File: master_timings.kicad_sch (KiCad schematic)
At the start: 9 parts, among them U1 74LS169BN, U11 TBP18s030, U12 74LS174N, U3 74F04, Y1 14 Mhz

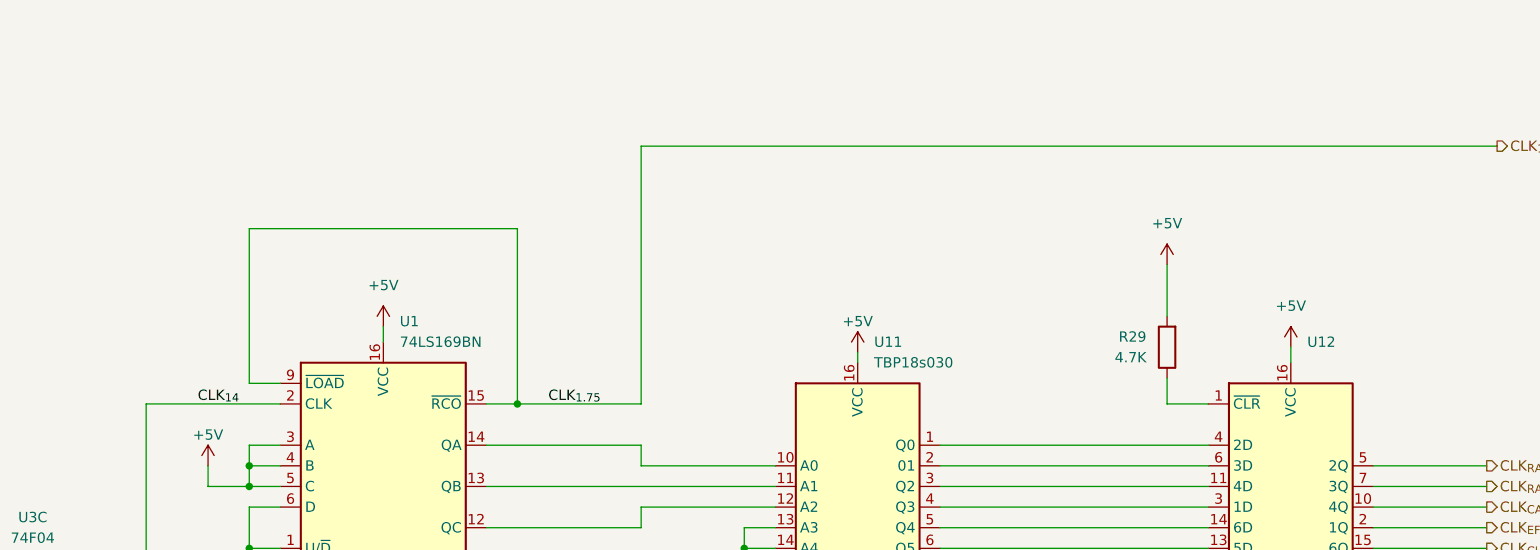
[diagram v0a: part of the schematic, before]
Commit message: Improved signal naming
clearer naming of some signals for better readability
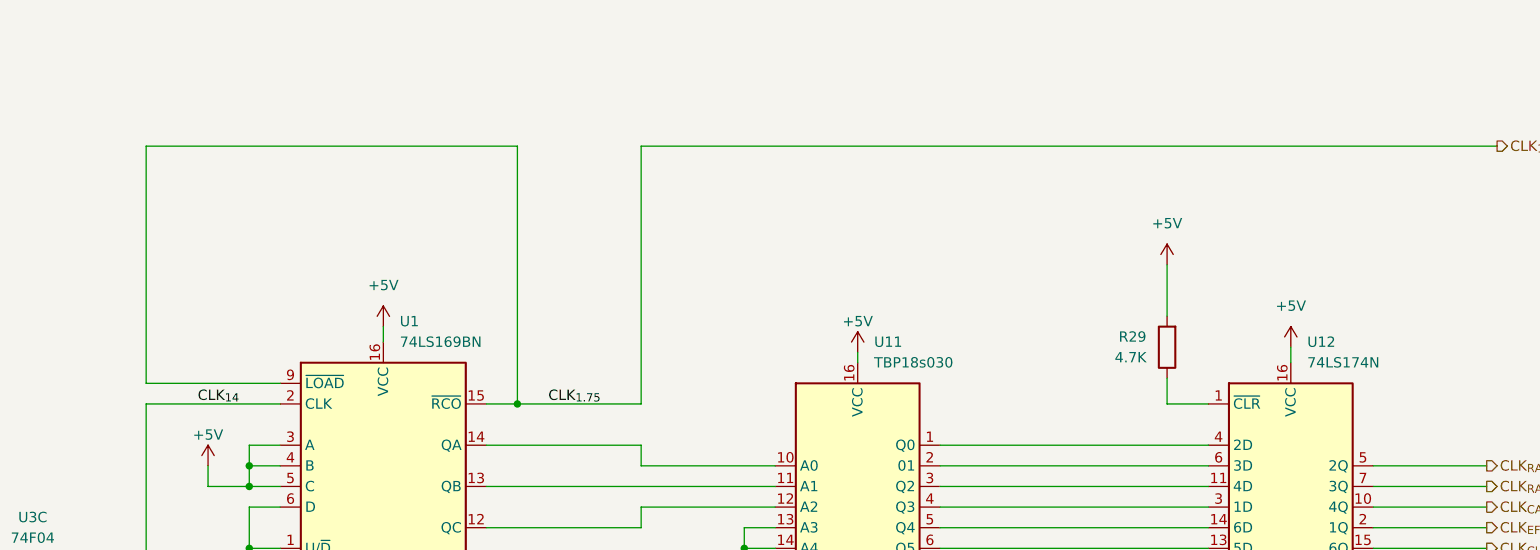
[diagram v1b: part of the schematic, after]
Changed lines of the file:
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@@
     (stroke (width 0) (type default))
   )
-  (wire (pts (xy 104.14 96.52) (xy 104.14 77.47))
+  (wire (pts (xy 91.44 96.52) (xy 91.44 67.31))
     (stroke (width 0) (type default))
   )
@@
     (stroke (width 0) (type default))
   )
-  (wire (pts (xy 104.14 96.52) (xy 107.95 96.52))
+  (wire (pts (xy 91.44 96.52) (xy 107.95 96.52))
     (stroke (width 0) (type default))
   )
@@
     (stroke (width 0) (type default))
   )
-  (wire (pts (xy 137.16 99.06) (xy 137.16 77.47))
+  (wire (pts (xy 137.16 99.06) (xy 137.16 67.31))
     (stroke (width 0) (type default))
   )
@@
     (stroke (width 0) (type default))
   )
-  (wire (pts (xy 104.14 77.47) (xy 137.16 77.47))
+  (wire (pts (xy 91.44 67.31) (xy 137.16 67.31))
     (stroke (width 0) (type default))
   )
@@
     )
     (property "Value" "74LS174N" (at 234.4294 93.98 0)
-      (effects (font (size 1.27 1.27)) (justify left) hide)
+      (effects (font (size 1.27 1.27)) (justify left))
     )
     (property "Footprint" "lsg_lib_fp:DIP-16_W7.62mm" (at 274.32 110.49 0)
